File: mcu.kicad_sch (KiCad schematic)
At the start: 38 parts, among them J2 Conn_01x10, J3 Conn_01x10, Q1 BC817, Q2 BC817, SW1 SW_Push, SW2 SW_Push, SW3 SW_Push, U4 ESP32-S3-WROOM-1, U5 CP2102N-A02-GQFN28R

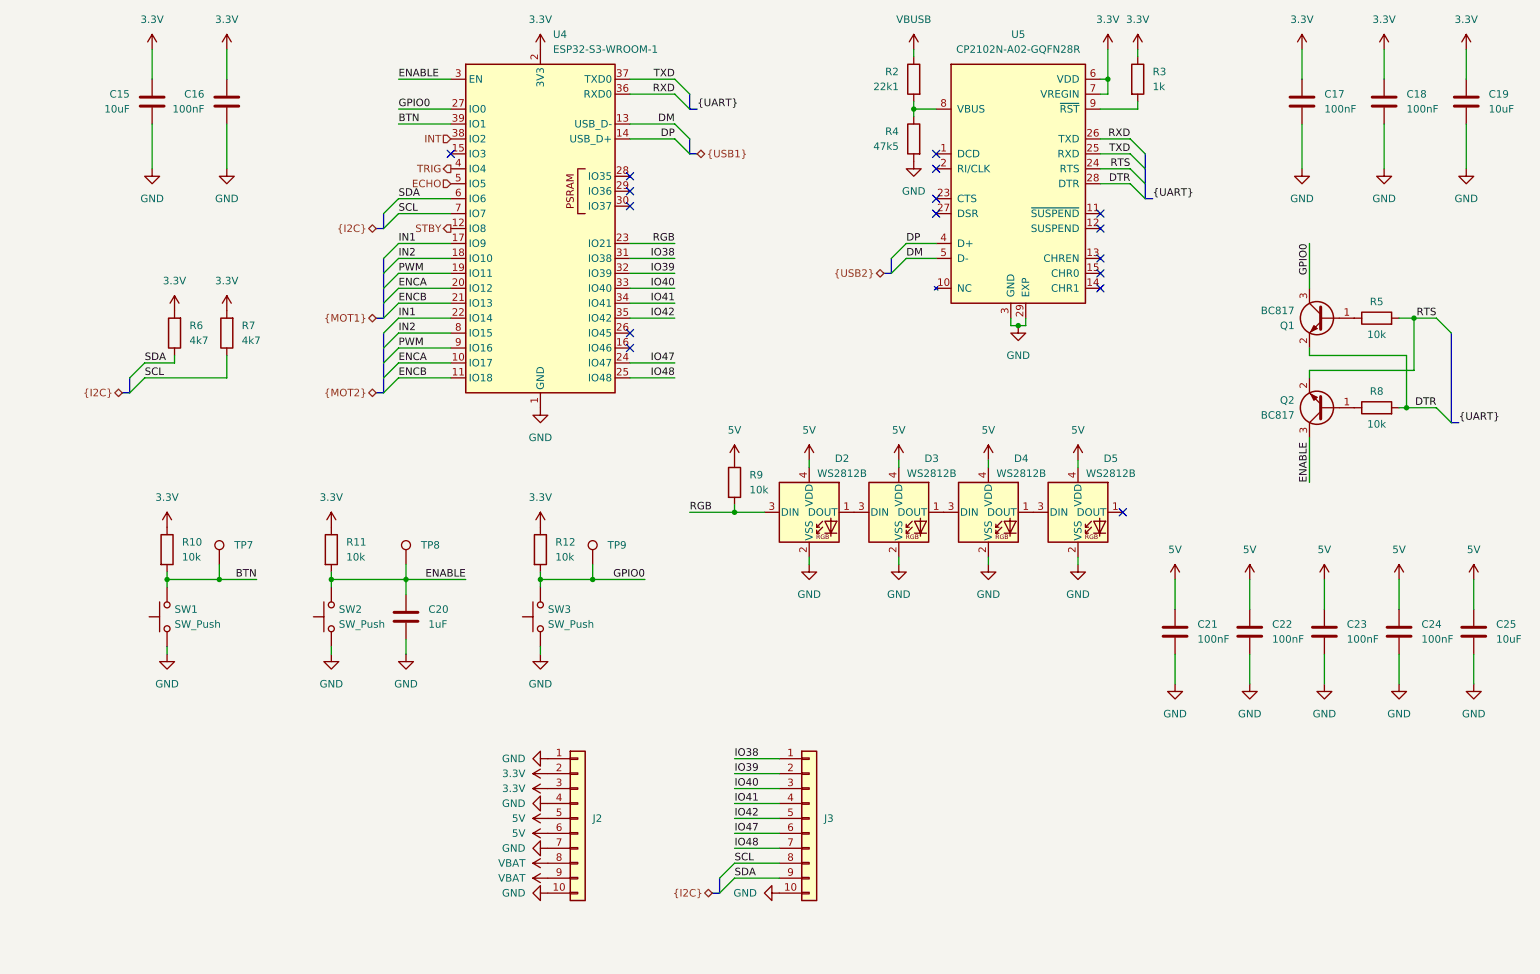
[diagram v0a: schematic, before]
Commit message: Break out ADC and touch pins
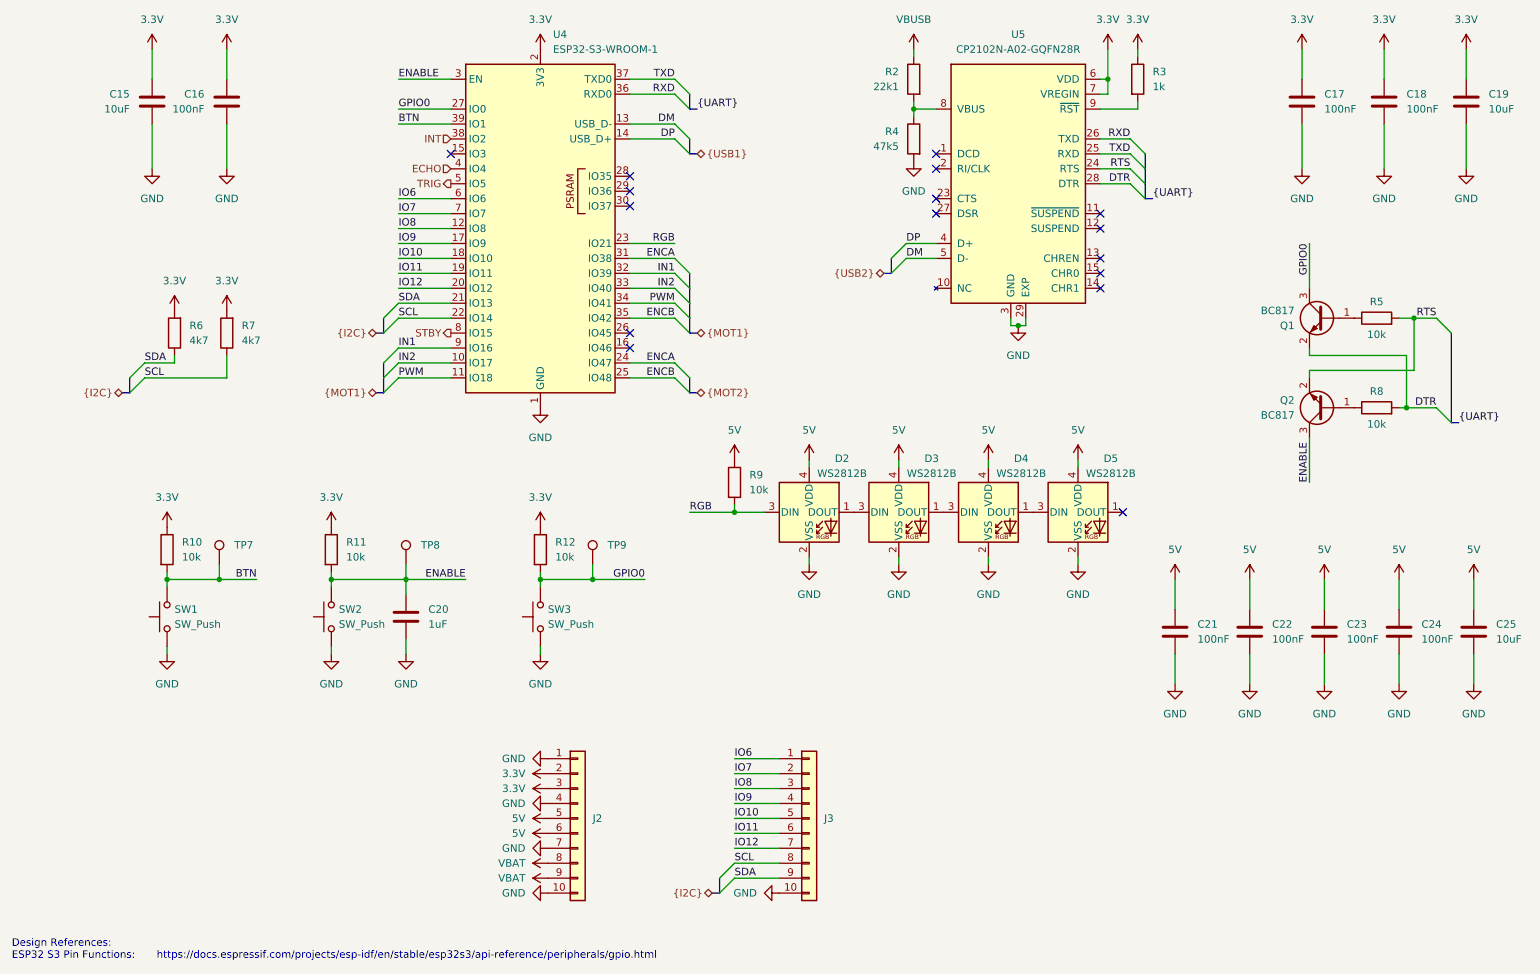
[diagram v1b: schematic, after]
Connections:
- net ECHO: now also U4.4 (IO4); no longer U4.5 (IO5)
- net ENCA: now also U4.24 (IO47), U4.31 (IO38); no longer U4.10 (IO17), U4.20 (IO12)
- net ENCB: now also U4.25 (IO48), U4.35 (IO42); no longer U4.11 (IO18), U4.21 (IO13)
- net IN1: now also U4.32 (IO39), U4.9 (IO16); no longer U4.17 (IO9), U4.22 (IO14)
- net IN2: now also U4.10 (IO17), U4.33 (IO40); no longer U4.18 (IO10), U4.8 (IO15)
- net PWM: now also U4.11 (IO18), U4.34 (IO41); no longer U4.19 (IO11), U4.9 (IO16)
- net SCL: now also U4.22 (IO14); no longer U4.7 (IO7)
- net SDA: now also U4.21 (IO13); no longer U4.6 (IO6)
- net STBY: now also U4.8 (IO15); no longer U4.12 (IO8)
- net TRIG: now also U4.5 (IO5); no longer U4.4 (IO4)
- net IO38 renamed IO6
- net IO6: now also U4.6 (IO6); no longer U4.31 (IO38)
- net IO39 renamed IO7
- net IO7: now also U4.7 (IO7); no longer U4.32 (IO39)
- net IO40 renamed IO8
- net IO8: now also U4.12 (IO8); no longer U4.33 (IO40)
- net IO41 renamed IO9
- net IO9: now also U4.17 (IO9); no longer U4.34 (IO41)
- net IO42 renamed IO10
- net IO10: now also U4.18 (IO10); no longer U4.35 (IO42)
- net IO47 renamed IO11
- net IO11: now also U4.19 (IO11); no longer U4.24 (IO47)
- net IO48 renamed IO12
- net IO12: now also U4.20 (IO12); no longer U4.25 (IO48)
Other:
- note added: "Design References: ESP32 S3 Pin Functions:"
- note added: "https://docs.espressif.com/projects/esp-idf/en/stable/esp32s3/api-reference/peripherals/gpio.html"

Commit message: Move fuse to correct location
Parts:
- renumbered TP7 to TP6, TP8 to TP7, TP9 to TP8
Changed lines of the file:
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@@
 		(dnp no)
 		(fields_autoplaced yes)
-		(property "Reference" "TP8"
+		(property "Reference" "TP7"
 			(at 86.36 123.6979 0)
 			(effects
@@
 			(project "Tumbler2_Redesign"
 				(path "/f3fd8d79-9d35-4c04-811e-2697a2740958/0ddd8726-a8b2-4557-84eb-e5ca9b362851"
-					(reference "TP8")
+					(reference "TP7")
 					(unit 1)
 				)
@@
 		(dnp no)
 		(fields_autoplaced yes)
-		(property "Reference" "TP9"
+		(property "Reference" "TP8"
 			(at 118.11 123.6979 0)
 			(effects
@@
 			(project "Tumbler2_Redesign"
 				(path "/f3fd8d79-9d35-4c04-811e-2697a2740958/0ddd8726-a8b2-4557-84eb-e5ca9b362851"
-					(reference "TP9")
+					(reference "TP8")
 					(unit 1)
 				)
@@
 		(dnp no)
 		(fields_autoplaced yes)
-		(property "Reference" "TP7"
+		(property "Reference" "TP6"
 			(at 54.61 123.6979 0)
 			(effects
@@
 			(project "Tumbler2_Redesign"
 				(path "/f3fd8d79-9d35-4c04-811e-2697a2740958/0ddd8726-a8b2-4557-84eb-e5ca9b362851"
-					(reference "TP7")
-					(unit 1)
-				)
+					(reference "TP6")
+					(unit 1)
+				)

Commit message: Assign footprints and parts
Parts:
- C15, C25: LCSC Part (none) -> C96446
- C16, C17, C18, C21, C22, C23, C24: footprint Capacitor_SMD:C_0402_1005Metric_Pad0.74x0.62mm_HandSolder -> Capacitor_SMD:C_0603_1608Metric_Pad1.08x0.95mm_HandSolder; LCSC Part (none) -> C14663
- C19: footprint Capacitor_SMD:C_0402_1005Metric_Pad0.74x0.62mm_HandSolder -> Capacitor_SMD:C_0603_1608Metric_Pad1.08x0.95mm_HandSolder; LCSC Part (none) -> C96446
- C20: footprint Capacitor_SMD:C_0402_1005Metric_Pad0.74x0.62mm_HandSolder -> Capacitor_SMD:C_0603_1608Metric_Pad1.08x0.95mm_HandSolder; LCSC Part (none) -> C29936
- J2, J3: LCSC Part (none) -> C5116489
- R10, R11, R12, R5, R8, R9: footprint (none) -> Resistor_SMD:R_0603_1608Metric_Pad0.98x0.95mm_HandSolder; LCSC Part (none) -> C98220
- R2: footprint (none) -> Resistor_SMD:R_0603_1608Metric_Pad0.98x0.95mm_HandSolder; LCSC Part (none) -> C137768
- R3: footprint (none) -> Resistor_SMD:R_0603_1608Metric_Pad0.98x0.95mm_HandSolder; LCSC Part (none) -> C22548
- R4: footprint (none) -> Resistor_SMD:R_0603_1608Metric_Pad0.98x0.95mm_HandSolder; LCSC Part (none) -> C137715
- R6, R7: footprint (none) -> Resistor_SMD:R_0603_1608Metric_Pad0.98x0.95mm_HandSolder; LCSC Part (none) -> C99782
- SW1, SW2, SW3: footprint (none) -> Tumbler2:SW_TS-1088-AR02016; LCSC Part (none) -> C720477
- TP6, TP7, TP8: footprint (none) -> TestPoint:TestPoint_Pad_D1.5mm

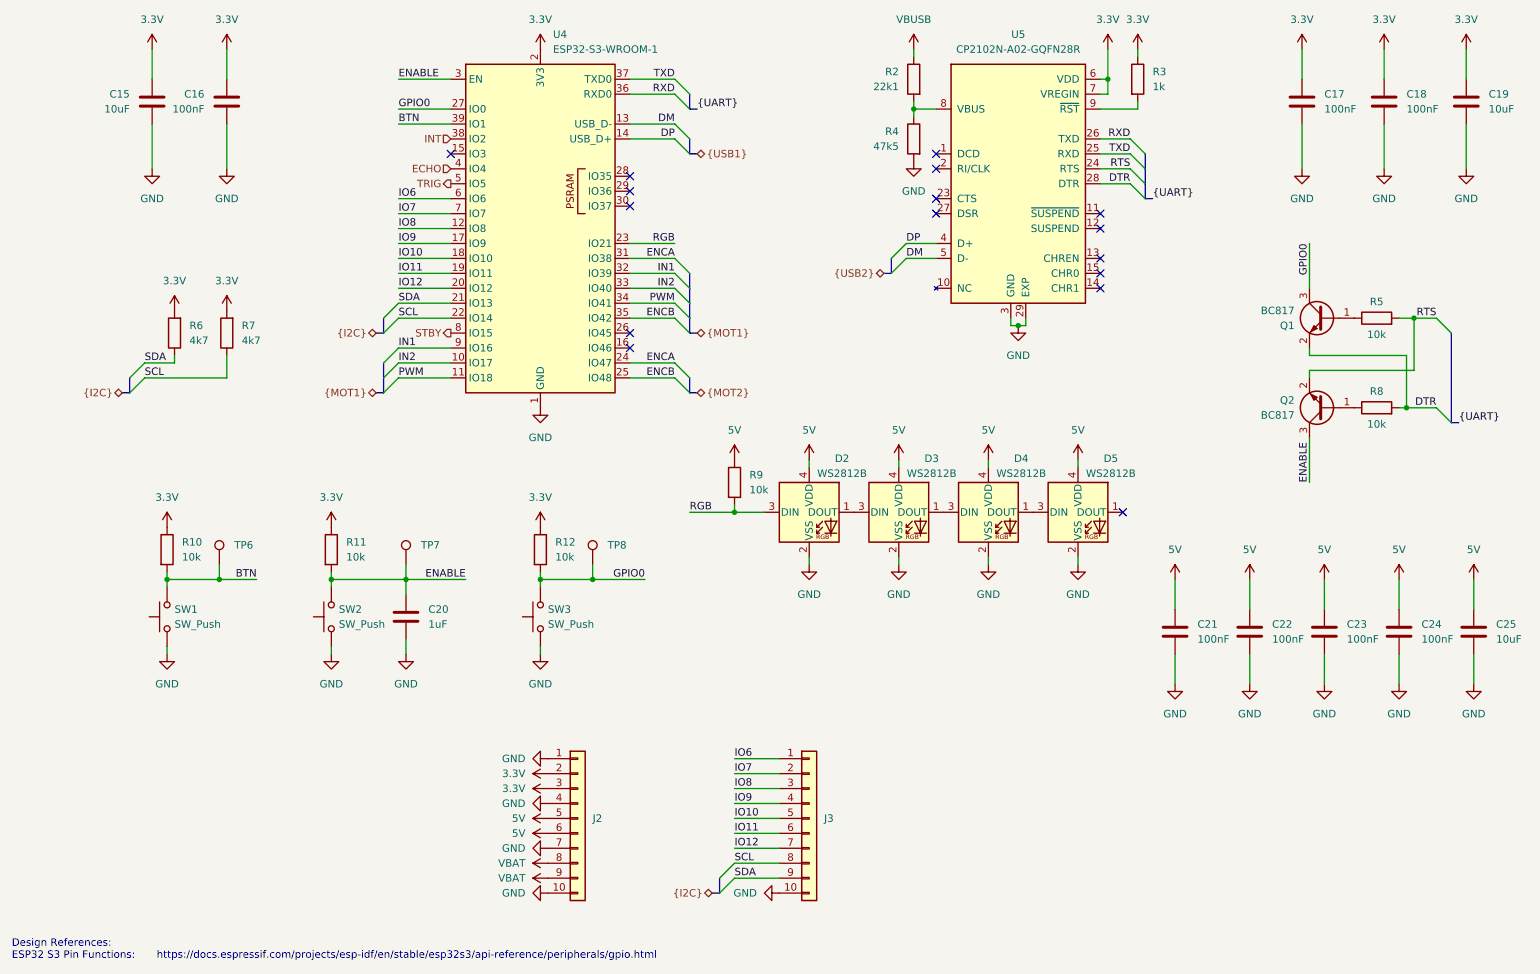
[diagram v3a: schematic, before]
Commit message: De-cascade buck converters
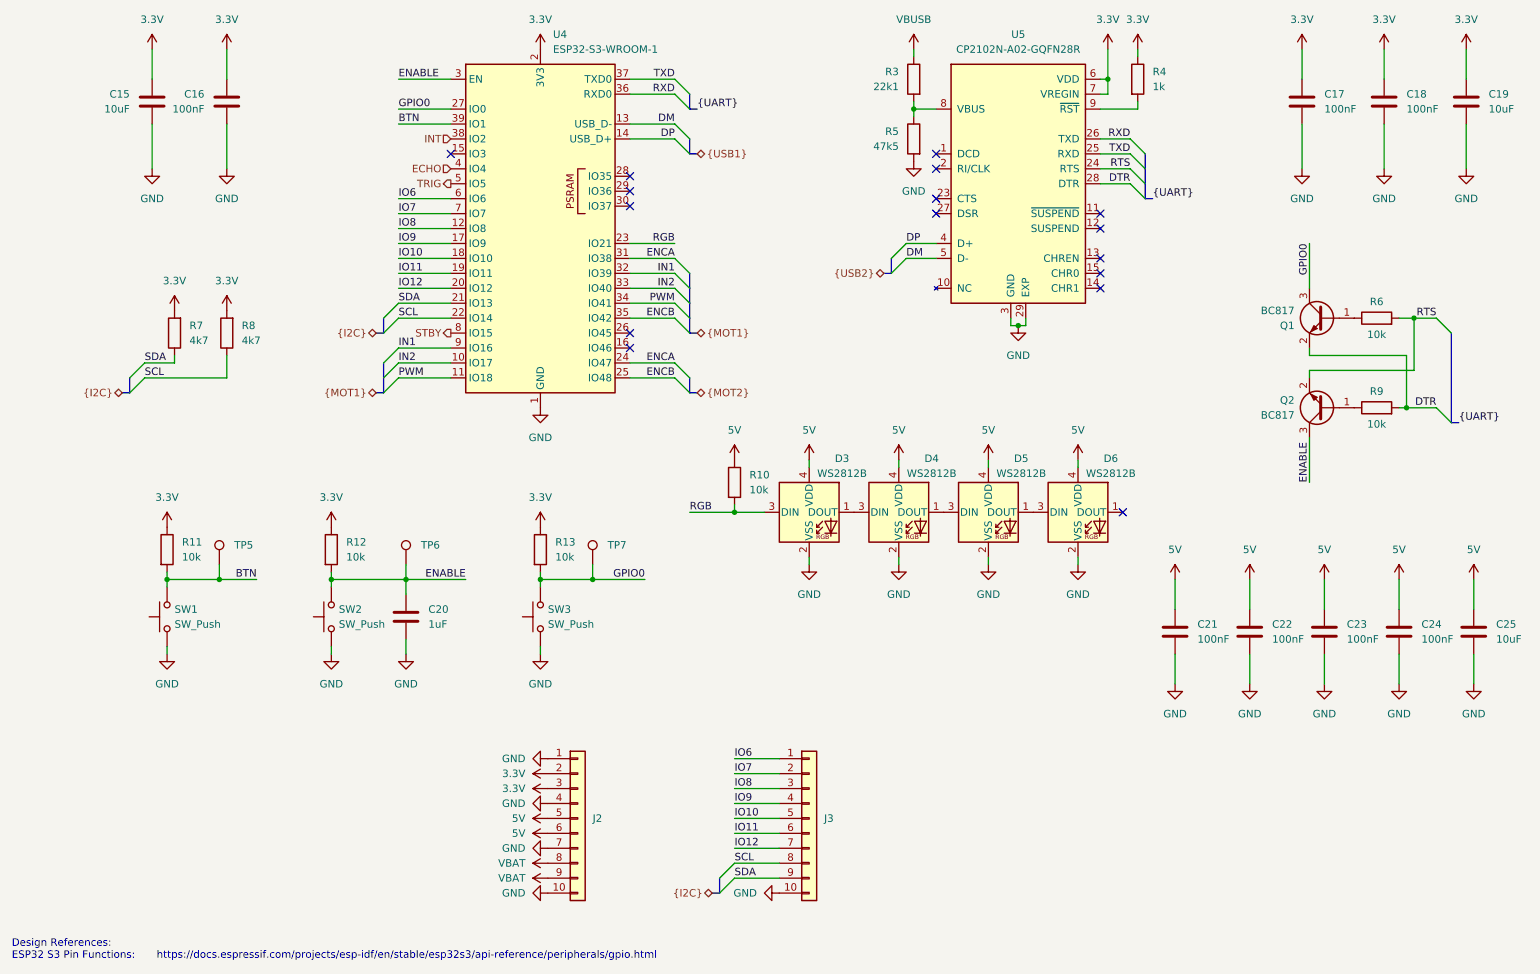
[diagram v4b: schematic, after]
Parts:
- renumbered D2 to D3, D3 to D4, D4 to D5, D5 to D6, R9 to R10, R10 to R11, R11 to R12, R12 to R13, R2 to R3, R3 to R4, R4 to R5, R5 to R6, R6 to R7, R7 to R8, R8 to R9, TP6 to TP5, TP7 to TP6, TP8 to TP7

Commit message: Break out motor encoder signals
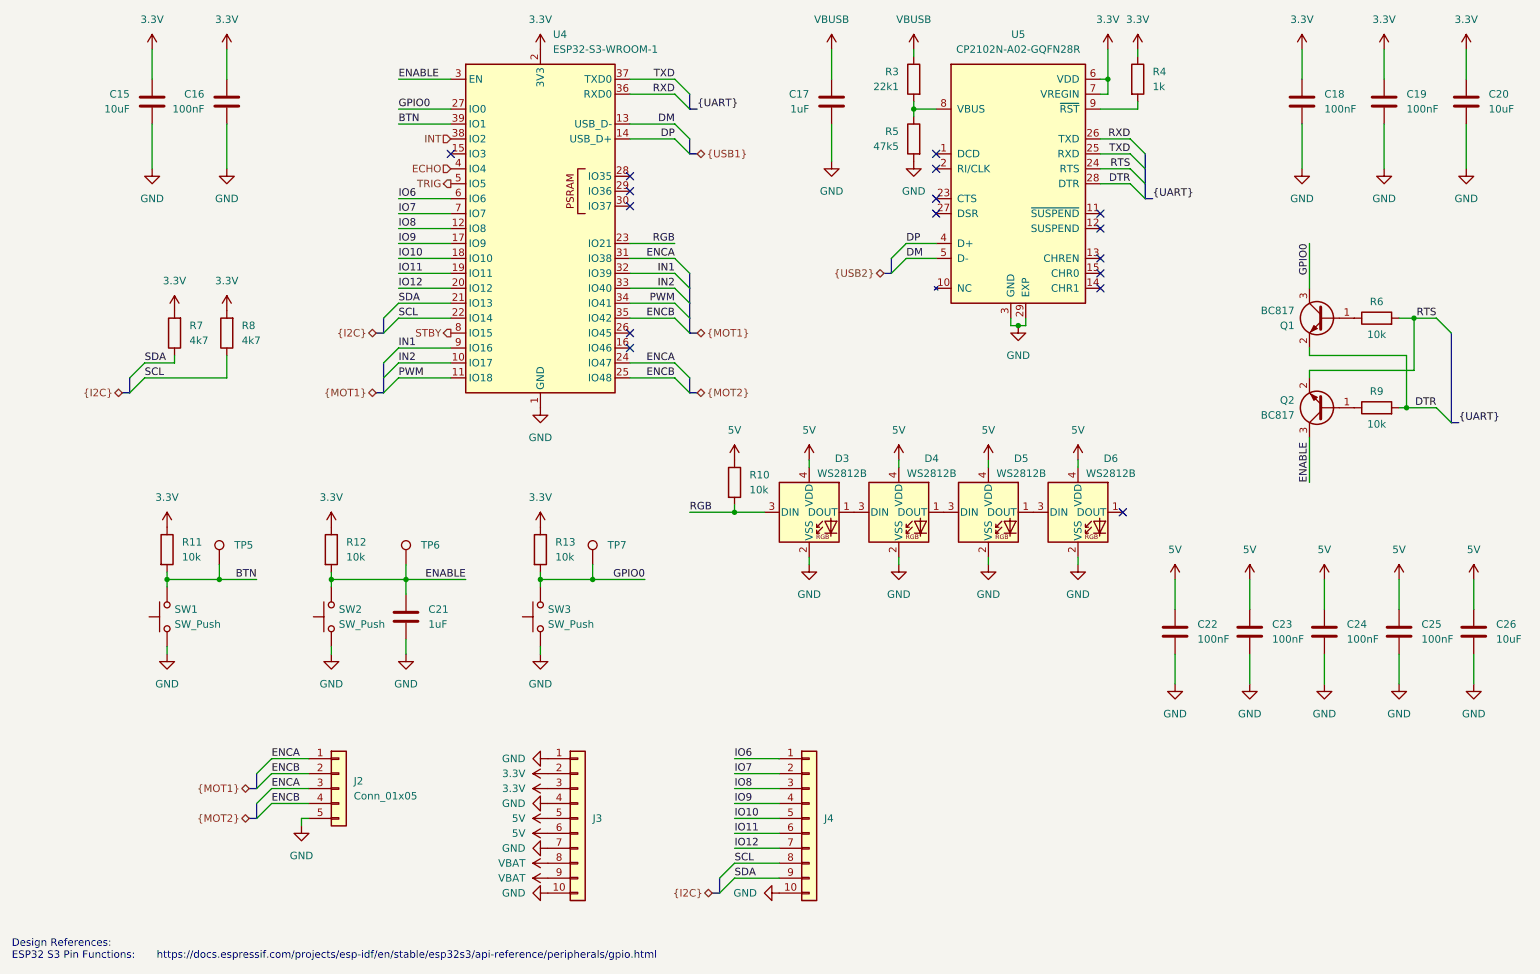
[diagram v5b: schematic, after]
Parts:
- added C17: 1uF, Capacitor_SMD:C_0603_1608Metric_Pad1.08x0.95mm_HandSolder, symbol Device:C
- added J2: Conn_01x05, Connector_PinHeader_2.54mm:PinHeader_1x05_P2.54mm_Vertical, symbol Connector_Generic:Conn_01x05
- renumbered C17 to C18, C18 to C19, C19 to C20, C20 to C21, C21 to C22, C22 to C23, C23 to C24, C24 to C25, C25 to C26, J2 to J3, J3 to J4
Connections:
- net ENCA: now also J2.1 (Pin_1), J2.3 (Pin_3)
- net ENCB: now also J2.2 (Pin_2), J2.4 (Pin_4)
- net GND: now also C17.2, J2.5 (Pin_5)
- net VBUSB: now also C17.1
